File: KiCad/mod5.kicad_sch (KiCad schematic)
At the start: 51 parts, among them M10 Fan_4pin, M9 Fan_4pin, U5 ZD25Q64BSIGT

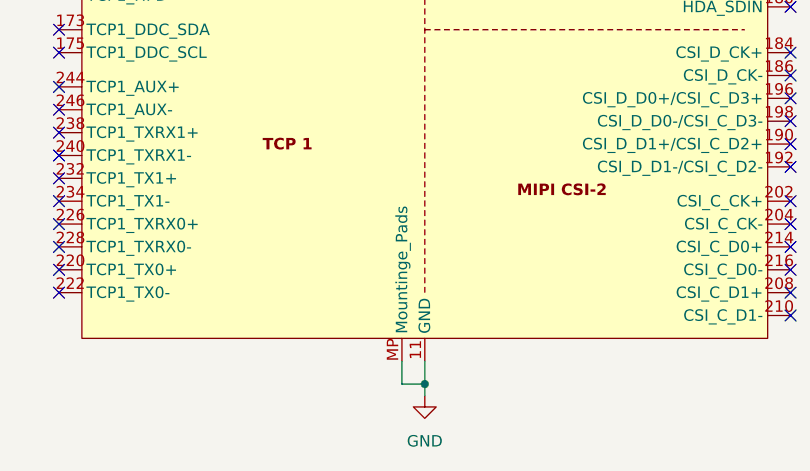
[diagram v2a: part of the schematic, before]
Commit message: Fix more footprint issues, continue laying out components
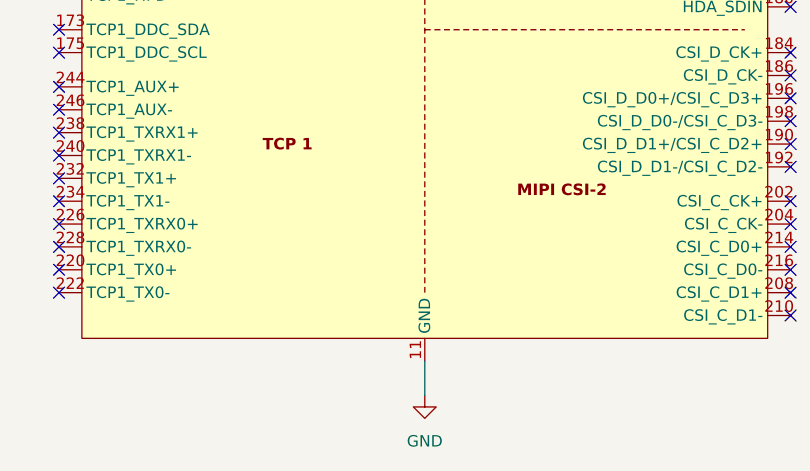
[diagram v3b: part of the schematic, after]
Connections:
- net GND: no longer A5.MP (Mountinge_Pads)
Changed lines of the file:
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@@
 	)
 	(junction
-		(at 276.86 340.36)
-		(diameter 0)
-		(color 0 0 0 0)
-	)
-	(junction
 		(at 386.08 45.72)
 		(diameter 0)
@@
 	(wire
 		(pts
-			(xy 276.86 337.82) (xy 276.86 340.36)
+			(xy 276.86 337.82) (xy 276.86 341.63)
 		)
 		(stroke
@@
 		)
 	)
-	(wire
-		(pts
-			(xy 276.86 340.36) (xy 276.86 341.63)
-		)
-		(stroke
-			(width 0)
-			(type default)
-		)
-	)
 	(bus
 		(pts
@@
 	(wire
 		(pts
-			(xy 274.32 340.36) (xy 276.86 340.36)
-		)
-		(stroke
-			(width 0)
-			(type default)
-		)
-	)
-	(wire
-		(pts
 			(xy 317.5 259.08) (xy 325.12 259.08)
 		)
@@
 		)
 	)
-	(wire
-		(pts
-			(xy 274.32 337.82) (xy 274.32 340.36)
-		)
-		(stroke
-			(width 0)
-			(type default)
-		)
-	)
 	(bus
 		(pts
@@
 		(pin "80"
 		)
-		(pin "MP"
-		)
 		(pin "256"

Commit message: Place STM32 and fix cpu fan headers
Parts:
- M9: footprint Connector:FanPinHeader_1x04_P2.54mm_Vertical -> Connector_JST:JST_PH_B4B-PH-K_1x04_P2.00mm_Vertical
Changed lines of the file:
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@@
 			)
 		)
-		(property "Footprint" "Connector:FanPinHeader_1x04_P2.54mm_Vertical"
+		(property "Footprint" "Connector_JST:JST_PH_B4B-PH-K_1x04_P2.00mm_Vertical"
 			(at 353.06 48.006 0)
 			(effects

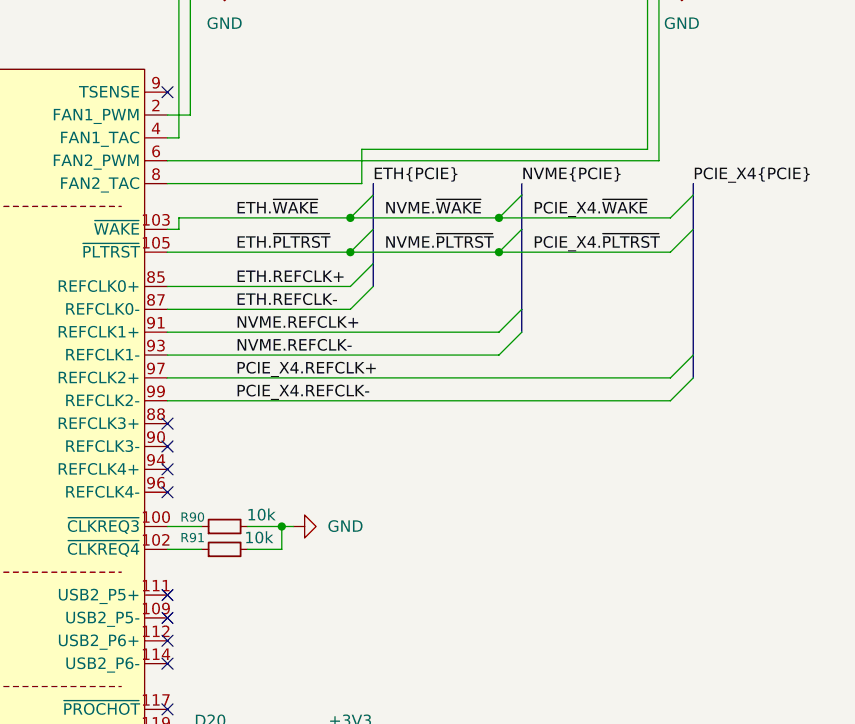
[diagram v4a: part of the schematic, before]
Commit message: Finish connecting x1 slot. Add pcie clkreq lines
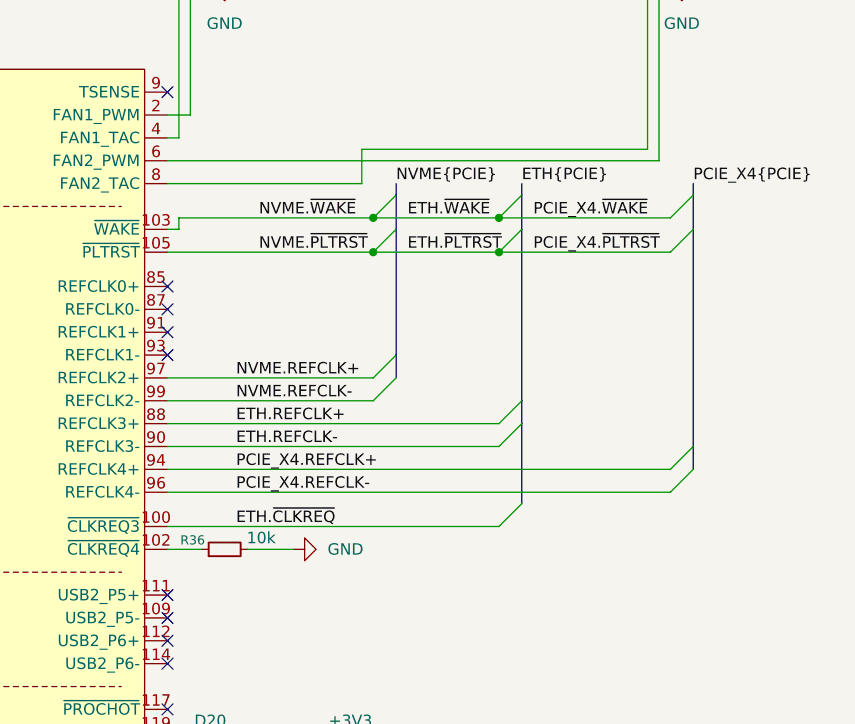
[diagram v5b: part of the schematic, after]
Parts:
- removed R90, R91: 10k, Resistor_SMD:R_0402_1005Metric, symbol Device:R_Small
- added R36: 10k, Resistor_SMD:R_0402_1005Metric, symbol Device:R_Small
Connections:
- net ETH.REFCLK+: now also A5.88 (REFCLK3+); no longer A5.85 (REFCLK0+)
- net ETH.REFCLK-: now also A5.90 (REFCLK3-); no longer A5.87 (REFCLK0-)
- net GND: now also R36.2
- net NVME.REFCLK+: now also A5.97 (REFCLK2+); no longer A5.91 (REFCLK1+)
- net NVME.REFCLK-: now also A5.99 (REFCLK2-); no longer A5.93 (REFCLK1-)
- net PCIE_X4.REFCLK+: now also A5.94 (REFCLK4+); no longer A5.97 (REFCLK2+)
- net PCIE_X4.REFCLK-: now also A5.96 (REFCLK4-); no longer A5.99 (REFCLK2-)
- net ETH.~{CLKREQ}: now reaches A5.100 (~{CLKREQ3})
- net at A5.102 (~{CLKREQ4}): now also R36.1

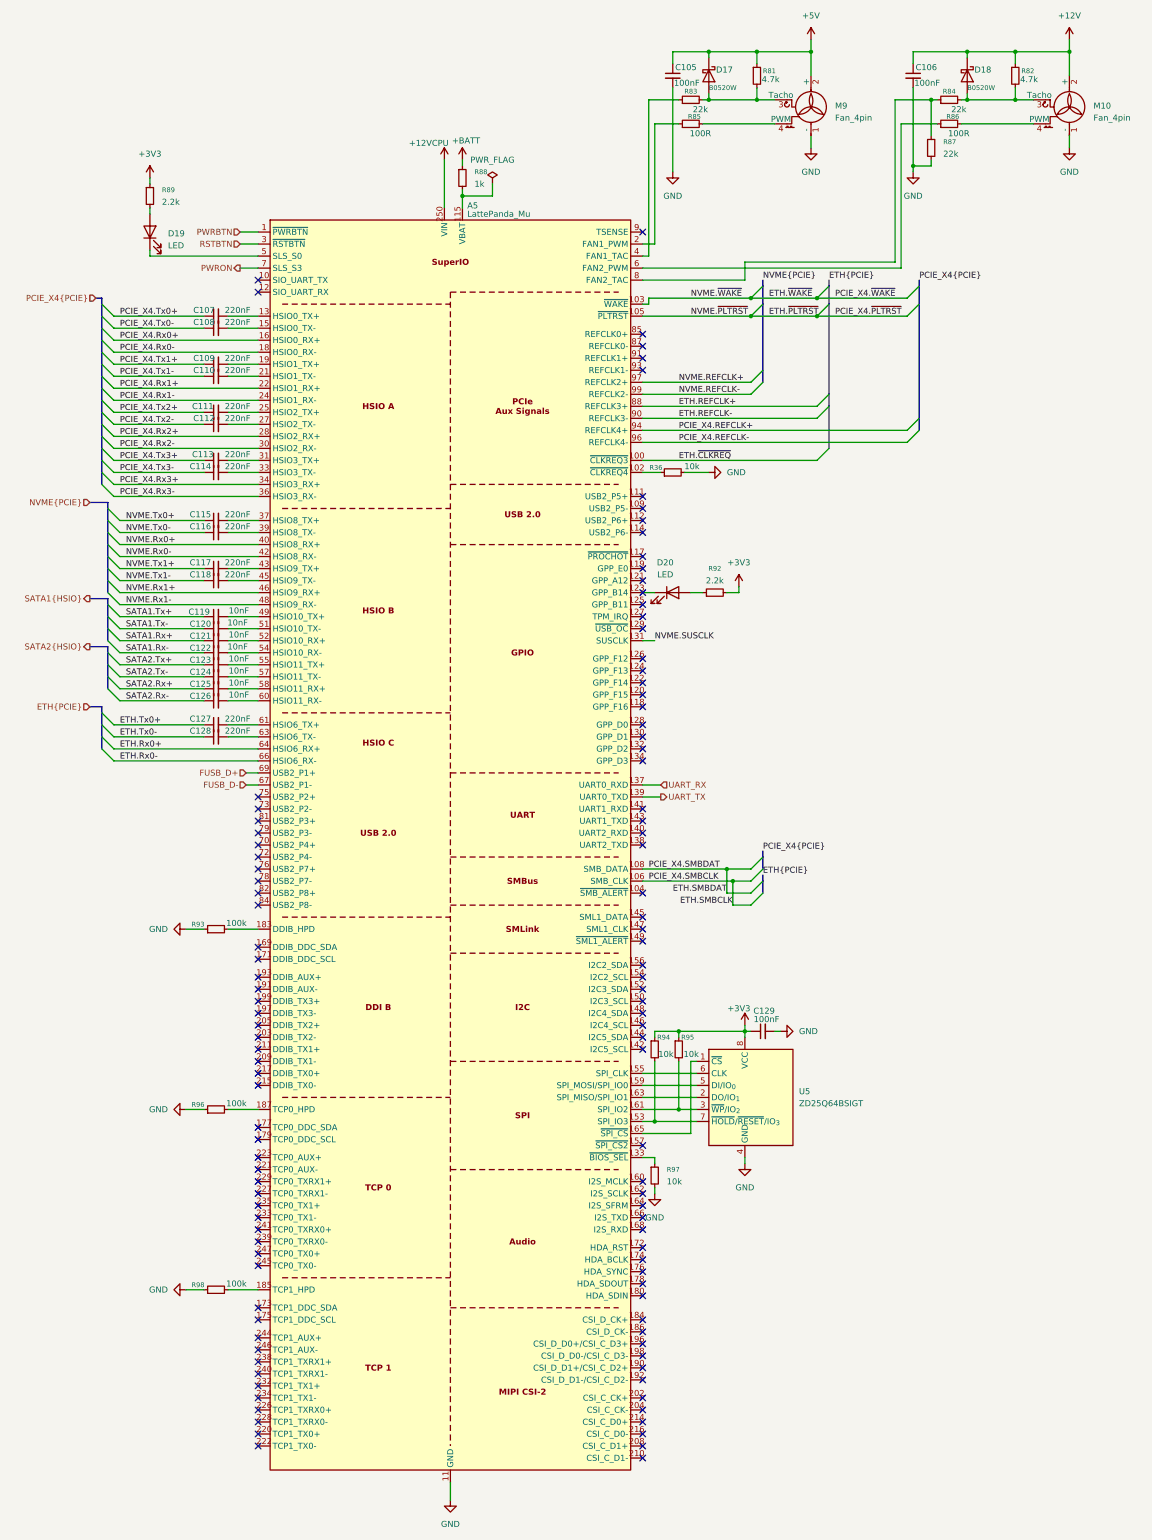
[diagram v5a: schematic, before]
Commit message: Re-annotate schematic
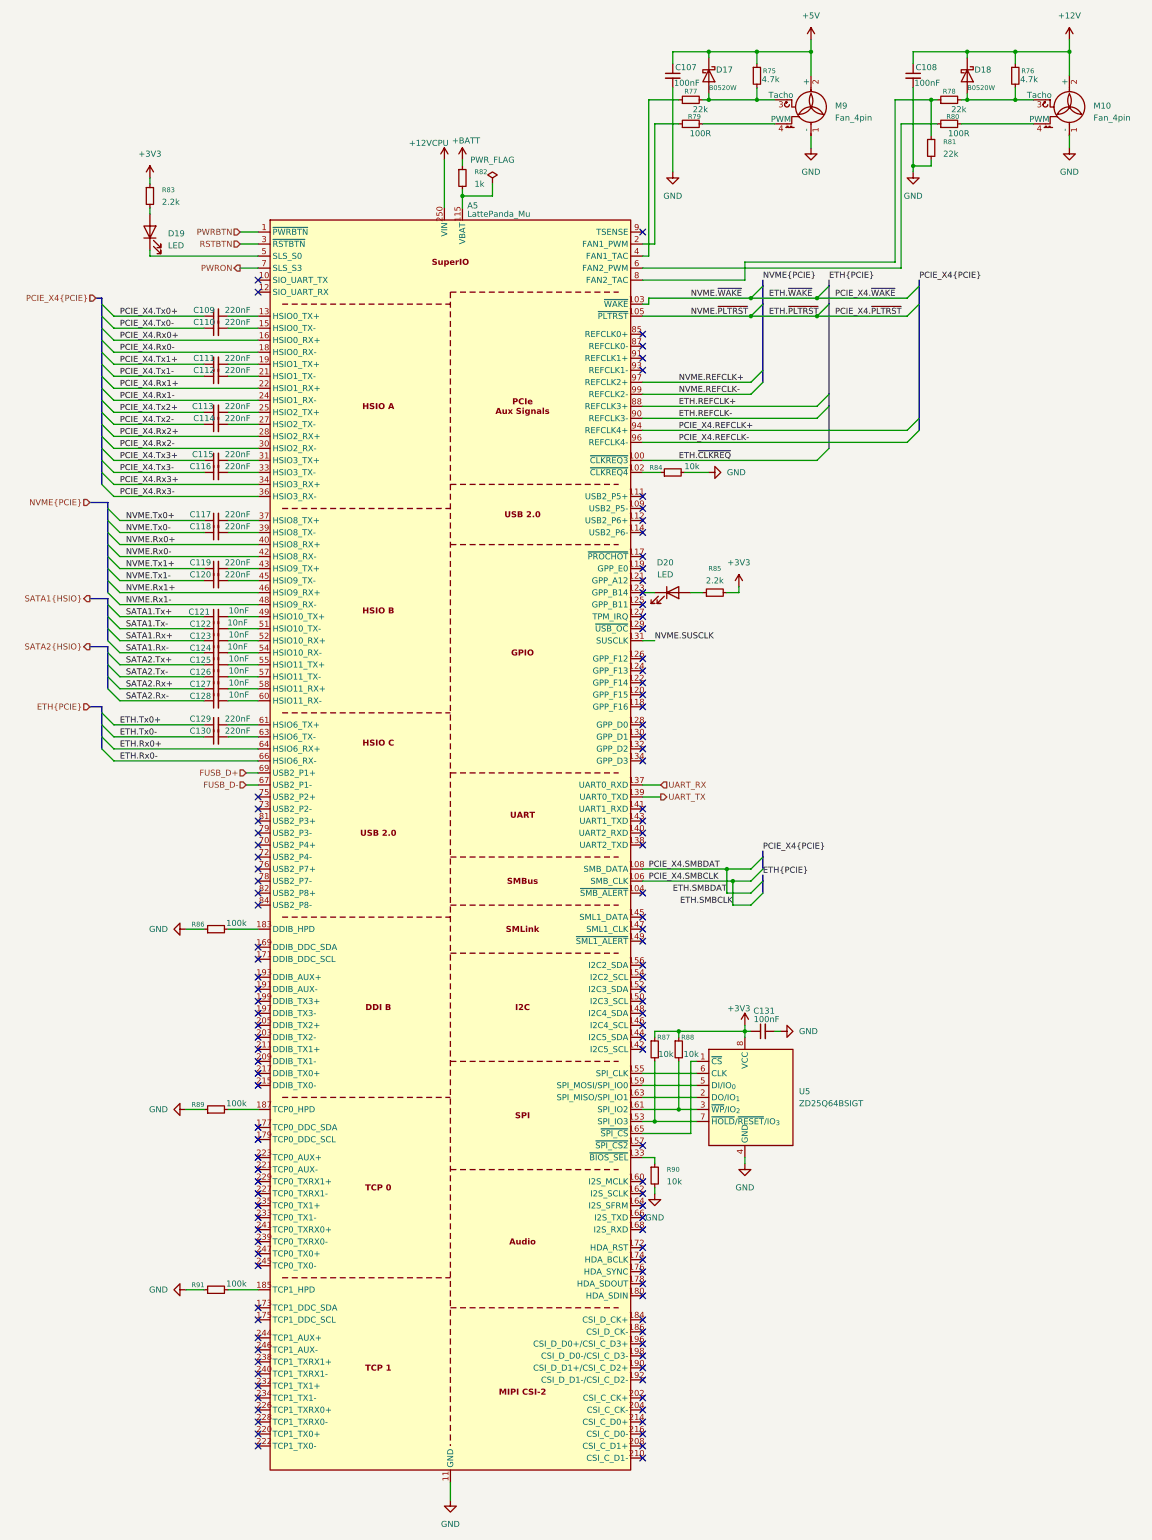
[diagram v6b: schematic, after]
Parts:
- renumbered C105 to C107, C106 to C108, C107 to C109, C108 to C110, C109 to C111, C110 to C112, C111 to C113, C112 to C114, C113 to C115, C114 to C116, C115 to C117, C116 to C118, C117 to C119, C118 to C120, C119 to C121, C120 to C122, C121 to C123, C122 to C124, C123 to C125, C124 to C126, C125 to C127, C126 to C128, C127 to C129, C128 to C130, C129 to C131, R81 to R75, R82 to R76, R83 to R77, R84 to R78, R85 to R79, R86 to R80, R87 to R81, R88 to R82, R89 to R83, R36 to R84, R92 to R85, R93 to R86, R94 to R87, R95 to R88, R96 to R89, R97 to R90, R98 to R91
